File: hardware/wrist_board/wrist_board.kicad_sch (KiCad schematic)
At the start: 56 parts, among them J1 S2B-PH-K-S_LF__SN_, J2 USB_C_Receptacle_USB2.0_14P, J3 Conn_01x02, J4 Conn_01x02, J5 Conn_01x02, J6 Conn_01x02, J7 Conn_01x02, J8 GPIOs, SW1 SW_SPST, SW2 BOOT_BTN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

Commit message: Added all JLC part numbers + generated production files
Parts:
- SW1: footprint Button_Switch_THT:SW_DIP_SPSTx01_Slide_6.7x4.1mm_W7.62mm_P2.54mm_LowProfile -> Button_Switch_SMD:SW_SPDT_Shouhan_MSK12C02
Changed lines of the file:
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@@
 			)
 		)
-		(property "Footprint" "Button_Switch_THT:SW_DIP_SPSTx01_Slide_6.7x4.1mm_W7.62mm_P2.54mm_LowProfile"
+		(property "Footprint" "Button_Switch_SMD:SW_SPDT_Shouhan_MSK12C02"
 			(at 100.33 129.54 0)
 			(effects

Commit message: Replaced old charging circuit, allows for input power derived from USB C or LIPO
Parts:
- removed U1: MCP73831T-2ACI_OT, MCP73831T-2ACI_OT:SOT95P280X145-5N, symbol MCP73831T-2ACI_OT:MCP73831T-2ACI_OT
- added C15: 10uF, Capacitor_SMD:C_0805_2012Metric, symbol Device:C_Small_US
- added R18: 46.4k, Resistor_SMD:R_0805_2012Metric, symbol Device:R_Small
- added R19: 10k, Resistor_SMD:R_0805_2012Metric, symbol Device:R_Small
- added R20: 1k, Resistor_SMD:R_0805_2012Metric, symbol Device:R_Small
- added U1: BQ24075RGT, Package_DFN_QFN:VQFN-16-1EP_3x3mm_P0.5mm_EP1.6x1.6mm, symbol Battery_Management:BQ24075RGT
- D1: value Charging LED -> CHG_LED
- R15, R16: value 10k -> 1k
- R3: value 10k -> 1.5k
- R4: value 470 -> 1.8k
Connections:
- net +5V: now also U1.13 (IN); no longer D1.2 (A)
- net GND: now also R4.2, C15.2, R18.2, R19.2, U1.15 (SYSOFF), U1.17 (VSS), U1.4 (~{CE}), U1.6 (EN1), U1.8 (VSS)
- net SYS: now reaches D1.1 (K)
- net SYS: now also SW1.1 (A), C15.1, U1.10 (OUT), U1.11 (OUT), U1.5 (EN2); no longer R4.2
- net at C10.1, C2.1, J1.1: now also U1.2 (BAT), U1.3 (BAT); no longer SW1.1 (A)
- net at R4.1: now also U1.16 (ISET)
- net at R3.1: now also U1.12 (ILIM)
- new net: R19.1, U1.1 (TS)
- new net: R18.1, U1.14 (TMR)
- new net: R20.1, U1.9 (~{CHG})
- new net: D1.2 (A), R20.2
- no-connect marks 23 -> 24
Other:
- moved on the sheet: C10, C2, J1

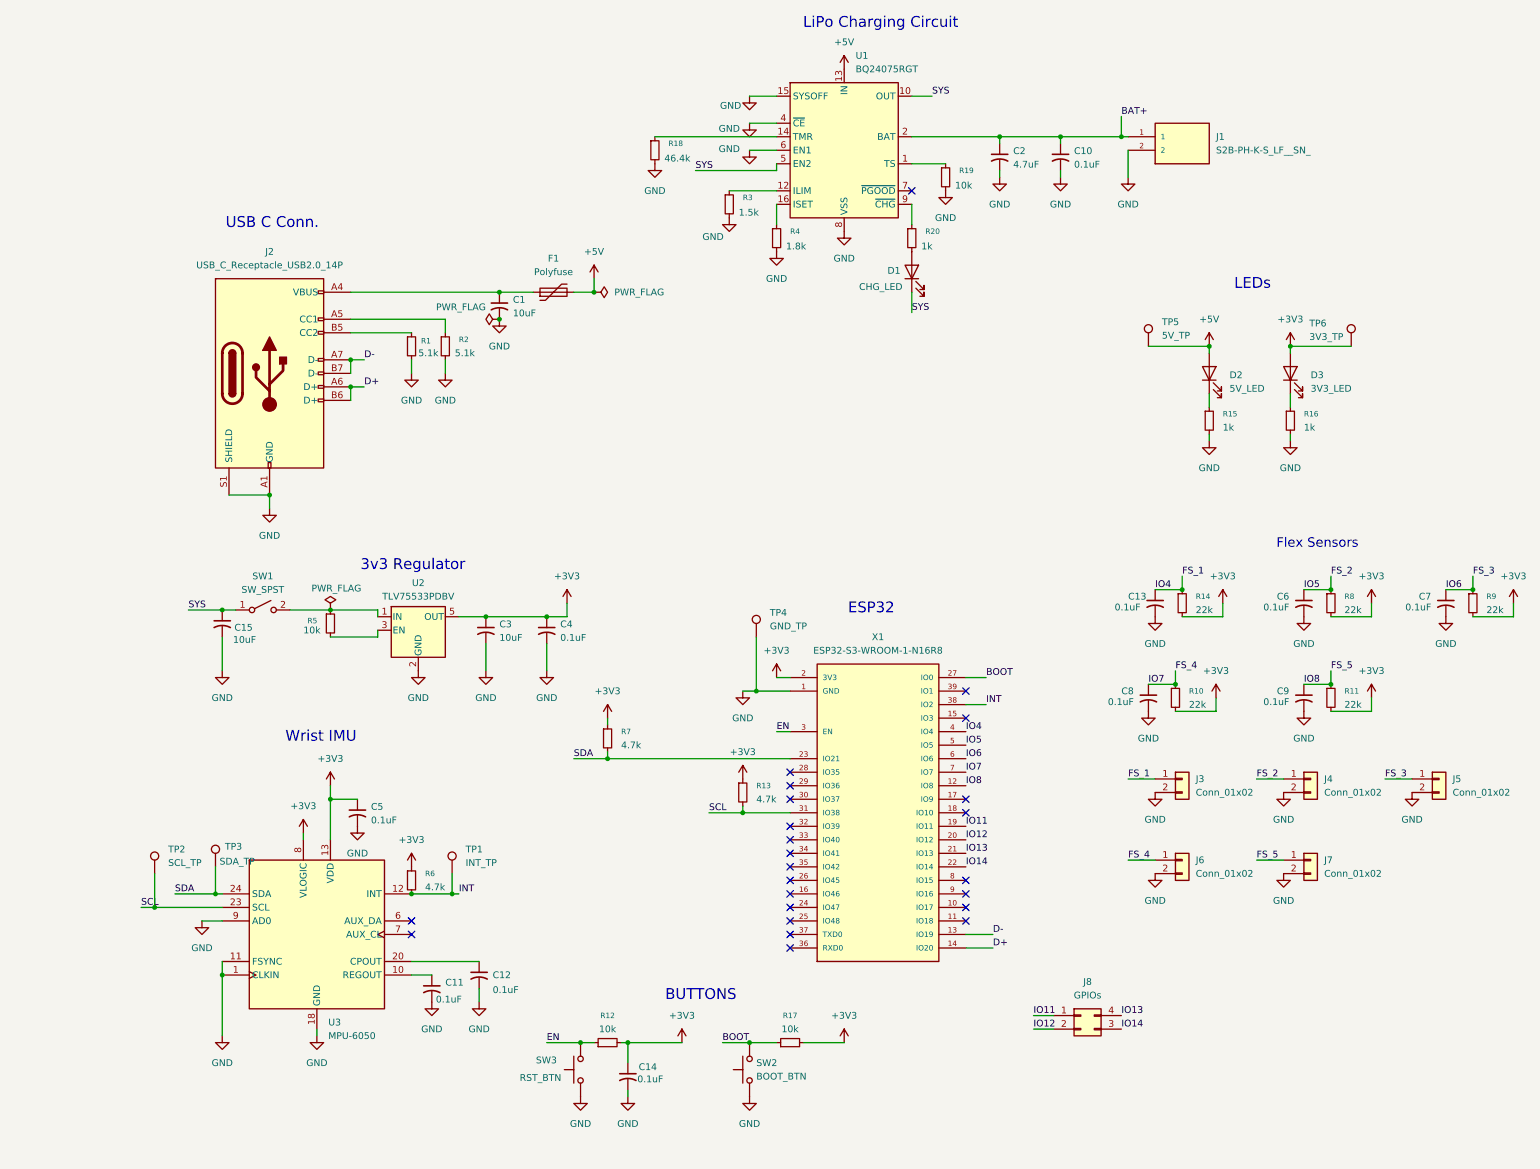
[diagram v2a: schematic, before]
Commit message: Replaced dupont headers with screw terminal
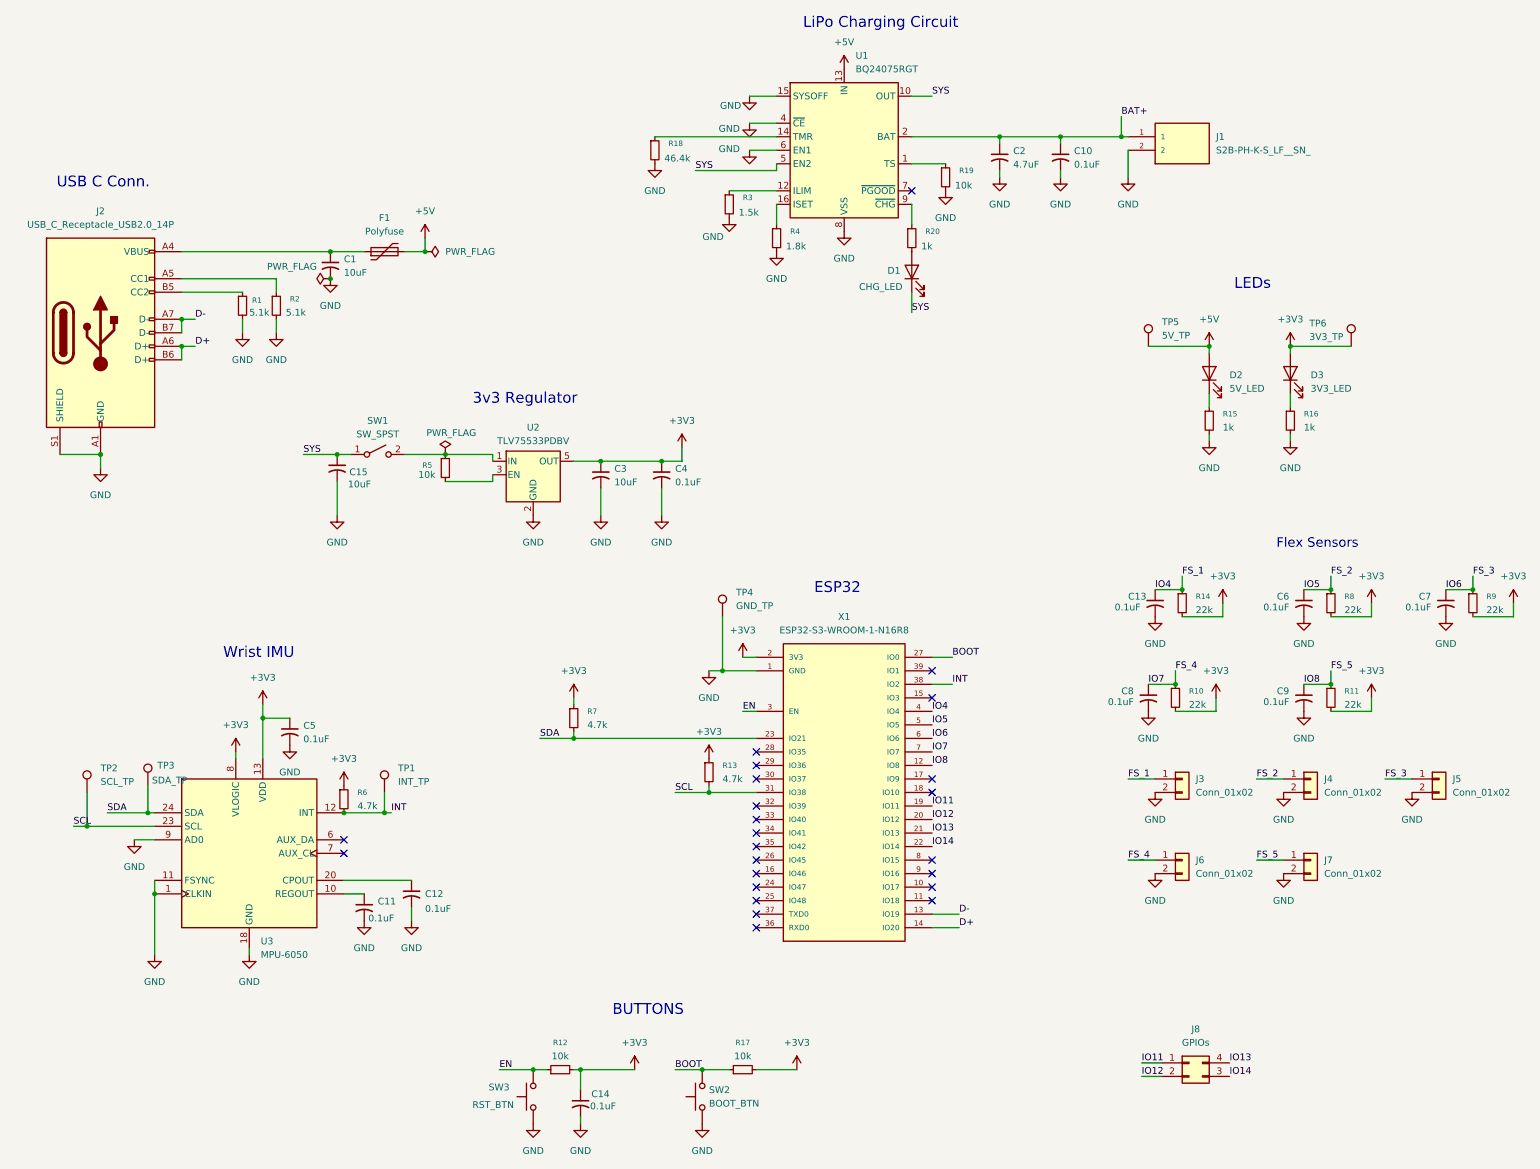
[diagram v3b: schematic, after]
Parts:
- J3, J4, J5, J6, J7: footprint Connector_PinHeader_2.54mm:PinHeader_1x02_P2.54mm_Horizontal -> easyeda2kicad:CONN-TH_DG350-3.5-02P-14-00A-H
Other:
- moved on the sheet: C1, C11, C12, C14, C15, C3, C4, C5, F1, J2, J8, R1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
